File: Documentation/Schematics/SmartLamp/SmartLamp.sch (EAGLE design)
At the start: 31 parts, among them J2 AVR_SPI_PROG_5X2PTH2, Q1 STN4NF03L, Q2 STN4NF03L, Q3 STN4NF03L, U1 MIC2920A, U2 DS3231MZ, U3 ATMEGA8/168/328, U4 HM-10

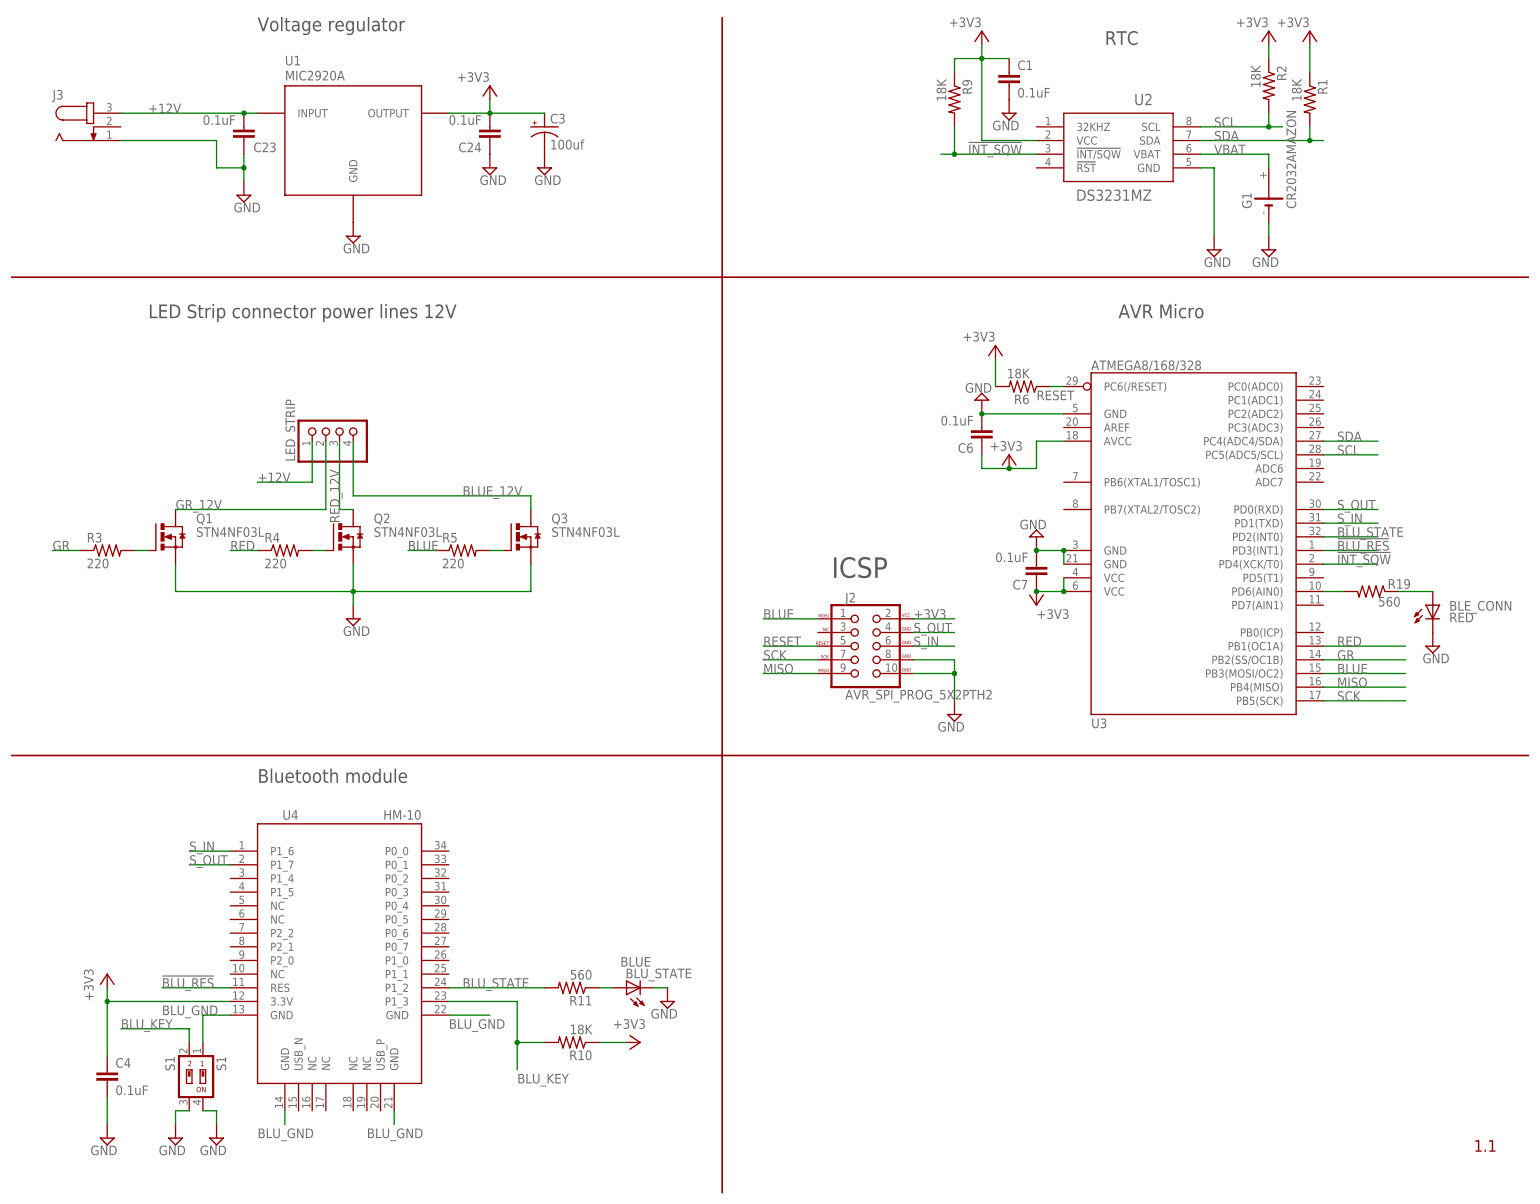
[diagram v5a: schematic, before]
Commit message: Fixed RX/?TX connection from micro to the BLE module.
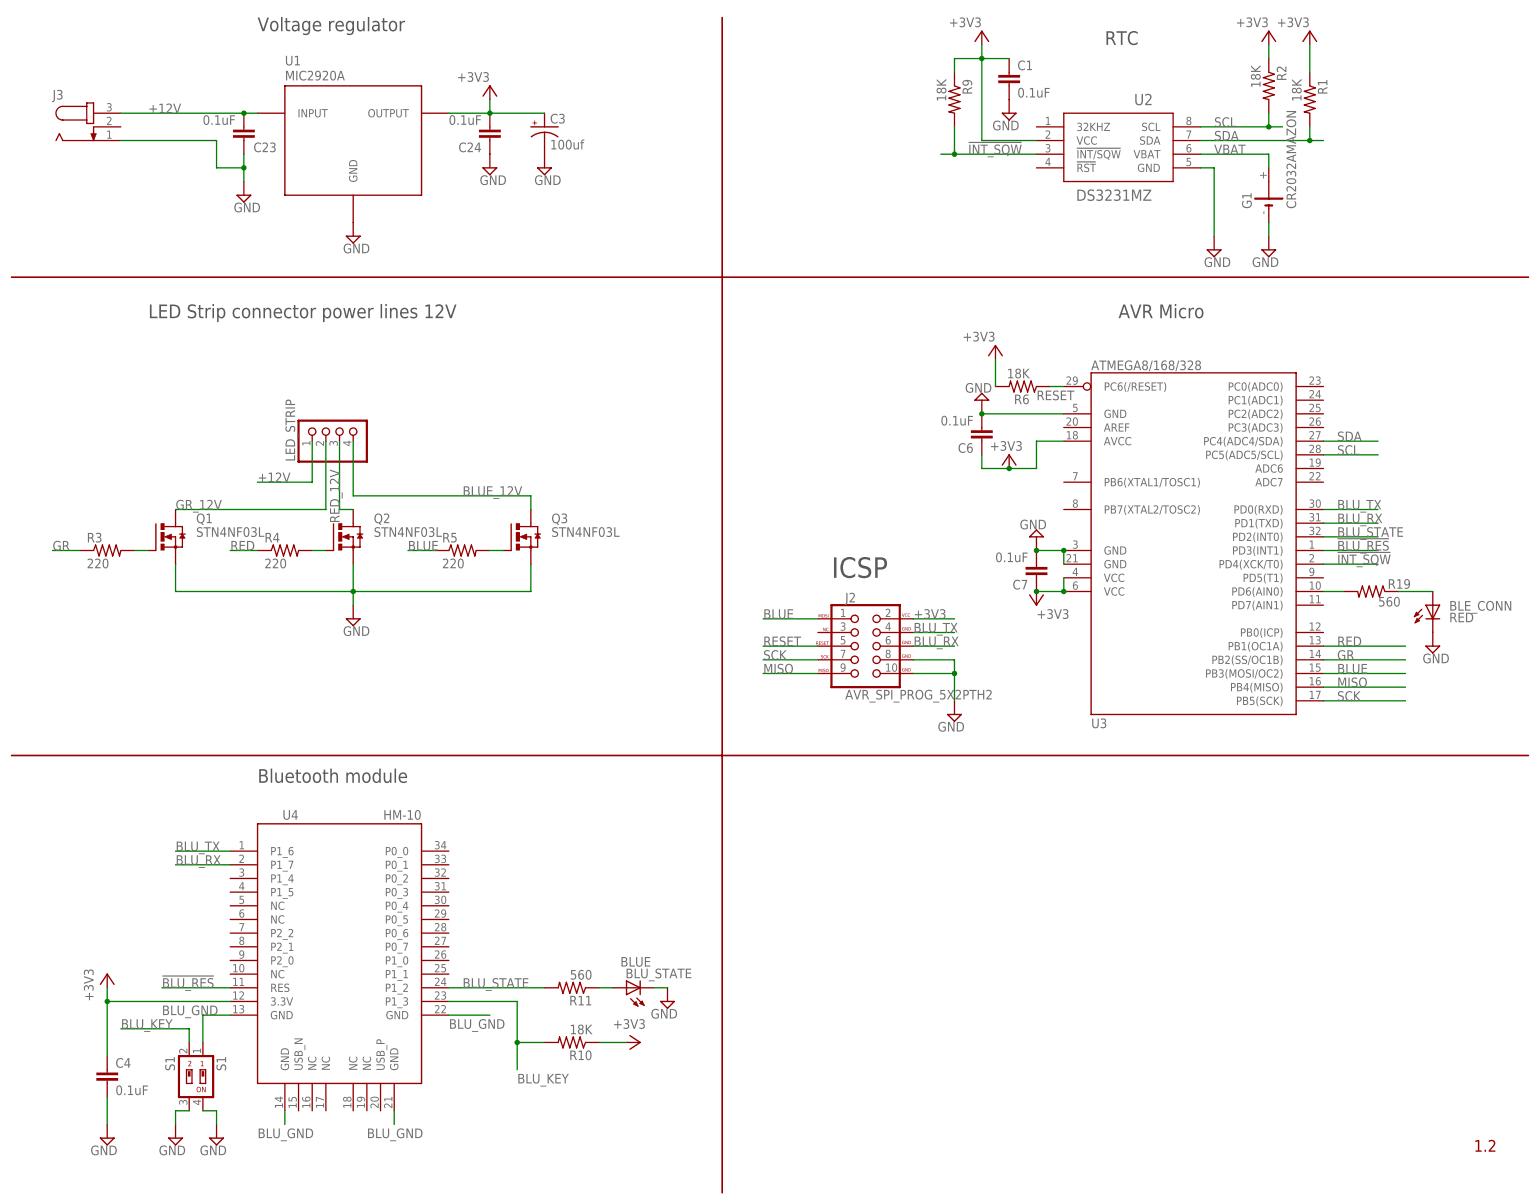
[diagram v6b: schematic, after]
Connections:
- removed net S_IN: J2.GND@2, U3.PD1(TXD), U4.P1_6
- removed net S_OUT: J2.GND@1, U3.PD0(RXD), U4.P1_7
- new net BLU_RX: J2.GND@2, U3.PD1(TXD), U4.P1_7
- new net BLU_TX: J2.GND@1, U3.PD0(RXD), U4.P1_6
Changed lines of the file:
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@@
 <schematic xreflabel="%F%N/%S" xrefpart="/%S.%C%R">
 <attributes>
-<attribute name="VERSION" value="1.1"/>
+<attribute name="VERSION" value="1.2"/>
 </attributes>
 <variantdefs>
@@
 </segment>
 </net>
-<net name="S_OUT" class="0">
-<segment>
-<pinref part="U4" gate="G$1" pin="P1_7"/>
-<wire x1="121.92" y1="66.04" x2="114.3" y2="66.04" width="0.1524" layer="91"/>
-<label x="114.3" y="66.04" size="1.778" layer="95" font="vector"/>
-</segment>
-<segment>
-<pinref part="U3" gate="G$1" pin="PD0(RXD)"/>
-<wire x1="325.12" y1="132.08" x2="335.28" y2="132.08" width="0.1524" layer="91"/>
-<label x="327.66" y="132.08" size="1.778" layer="95" font="vector"/>
-</segment>
-<segment>
-<pinref part="J2" gate="G$1" pin="GND@1"/>
-<wire x1="248.92" y1="109.22" x2="256.54" y2="109.22" width="0.1524" layer="91"/>
-<label x="248.92" y="109.22" size="1.778" layer="95" font="vector"/>
-</segment>
-</net>
 <net name="SCK" class="0">
 <segment>
@@
 <wire x1="345.44" y1="116.84" x2="339.09" y2="116.84" width="0.1524" layer="91"/>
 <pinref part="BLE_CONN" gate="G$1" pin="A"/>
-</segment>
-</net>
-<net name="S_IN" class="0">
-<segment>
-<pinref part="U4" gate="G$1" pin="P1_6"/>
-<wire x1="121.92" y1="68.58" x2="114.3" y2="68.58" width="0.1524" layer="91"/>
-<label x="114.3" y="68.58" size="1.778" layer="95" font="vector"/>
-</segment>
-<segment>
-<pinref part="U3" gate="G$1" pin="PD1(TXD)"/>
-<wire x1="325.12" y1="129.54" x2="335.28" y2="129.54" width="0.1524" layer="91"/>
-<label x="327.66" y="129.54" size="1.778" layer="95" font="vector"/>
-</segment>
-<segment>
-<pinref part="J2" gate="G$1" pin="GND@2"/>
-<wire x1="248.92" y1="106.68" x2="256.54" y2="106.68" width="0.1524" layer="91"/>
-<label x="248.92" y="106.68" size="1.778" layer="95" font="vector"/>
 </segment>
 </net>
@@
 </segment>
 </net>
+<net name="BLU_TX" class="0">
+<segment>
+<pinref part="U4" gate="G$1" pin="P1_6"/>
+<wire x1="121.92" y1="68.58" x2="111.76" y2="68.58" width="0.1524" layer="91"/>
+<label x="111.76" y="68.58" size="1.778" layer="95" font="vector"/>
+</segment>
+<segment>
+<pinref part="U3" gate="G$1" pin="PD0(RXD)"/>
+<wire x1="325.12" y1="132.08" x2="335.28" y2="132.08" width="0.1524" layer="91"/>
+<label x="327.66" y="132.08" size="1.778" layer="95" font="vector"/>
+</segment>
+<segment>
+<pinref part="J2" gate="G$1" pin="GND@1"/>
+<wire x1="248.92" y1="109.22" x2="256.54" y2="109.22" width="0.1524" layer="91"/>
+<label x="248.92" y="109.22" size="1.778" layer="95" font="vector"/>
+</segment>
+</net>
+<net name="BLU_RX" class="0">
+<segment>
+<pinref part="U4" gate="G$1" pin="P1_7"/>
+<wire x1="121.92" y1="66.04" x2="111.76" y2="66.04" width="0.1524" layer="91"/>
+<label x="111.76" y="66.04" size="1.778" layer="95" font="vector"/>
+</segment>
+<segment>
+<pinref part="U3" gate="G$1" pin="PD1(TXD)"/>
+<wire x1="325.12" y1="129.54" x2="335.28" y2="129.54" width="0.1524" layer="91"/>
+<label x="327.66" y="129.54" size="1.778" layer="95" font="vector"/>
+</segment>
+<segment>
+<pinref part="J2" gate="G$1" pin="GND@2"/>
+<wire x1="248.92" y1="106.68" x2="256.54" y2="106.68" width="0.1524" layer="91"/>
+<label x="248.92" y="106.68" size="1.778" layer="95" font="vector"/>
+</segment>
+</net>

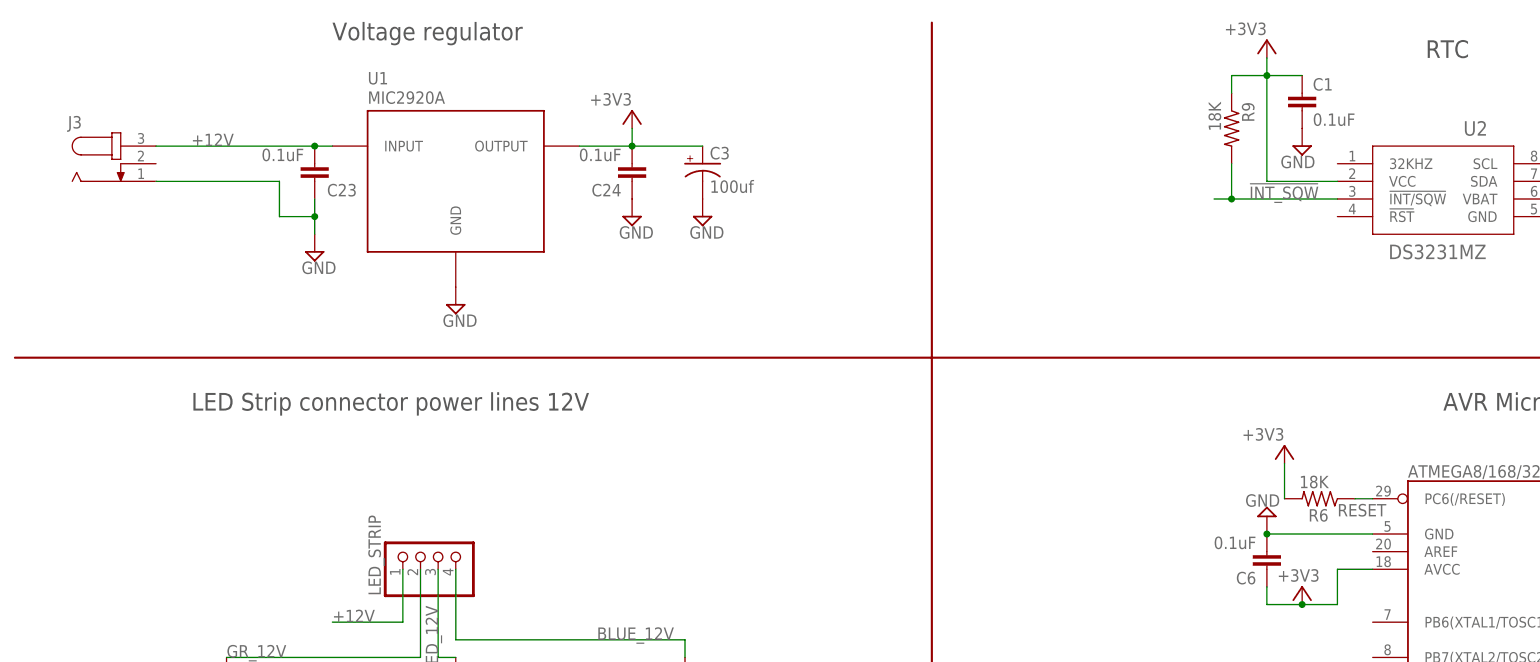
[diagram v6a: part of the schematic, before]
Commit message: Added micro reset button.
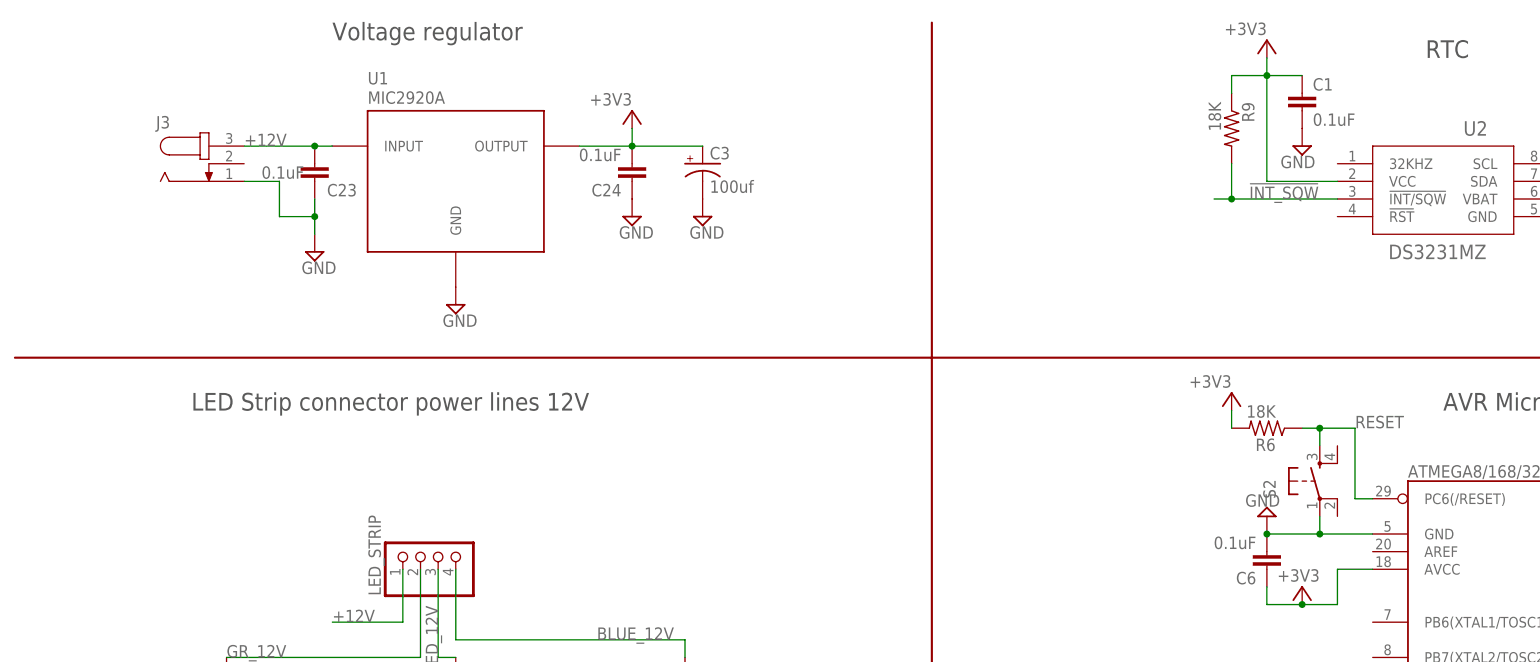
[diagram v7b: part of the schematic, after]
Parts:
- added S2: DTSM-6, switch-tact:DTSM-6
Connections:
- net GND: now also S2.1
- net RESET: now also S2.3
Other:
- moved on the sheet: J3, R6
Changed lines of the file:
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@@
 <part name="GND5" library="supply2" deviceset="GND" device=""/>
 <part name="J3" library="con-jack" deviceset="JACK-PLUG" device="0"/>
+<part name="S2" library="switch-tact" deviceset="DTSM-6" device=""/>
 </parts>
 <sheets>
@@
 <instance part="C23" gate="G$1" x="124.46" y="200.66" smashed="yes" rot="R180">
 <attribute name="NAME" x="130.556" y="200.279" size="1.778" layer="95" rot="R180"/>
-<attribute name="VALUE" x="122.936" y="205.359" size="1.778" layer="96" rot="R180"/>
+<attribute name="VALUE" x="122.936" y="202.819" size="1.778" layer="96" rot="R180"/>
 </instance>
 <instance part="C24" gate="G$1" x="170.18" y="200.66" rot="R180"/>
@@
 <instance part="Q2" gate="G$1" x="142.24" y="127"/>
 <instance part="Q3" gate="G$1" x="175.26" y="127"/>
-<instance part="R6" gate="G$1" x="269.24" y="154.94" smashed="yes" rot="R180">
-<attribute name="NAME" x="270.51" y="153.4414" size="1.778" layer="95" rot="R180"/>
-<attribute name="VALUE" x="270.51" y="158.242" size="1.778" layer="96" rot="R180"/>
-</instance>
-<instance part="+3V1" gate="G$1" x="264.16" y="162.56" smashed="yes">
-<attribute name="VALUE" x="264.16" y="165.1" size="1.778" layer="96" rot="R180"/>
+<instance part="R6" gate="G$1" x="261.62" y="165.1" smashed="yes" rot="R180">
+<attribute name="NAME" x="262.89" y="163.6014" size="1.778" layer="95" rot="R180"/>
+<attribute name="VALUE" x="262.89" y="168.402" size="1.778" layer="96" rot="R180"/>
+</instance>
+<instance part="+3V1" gate="G$1" x="256.54" y="170.18" smashed="yes">
+<attribute name="VALUE" x="256.54" y="172.72" size="1.778" layer="96" rot="R180"/>
 </instance>
 <instance part="C3" gate="G$1" x="180.34" y="203.2"/>
@@
 <instance part="J2" gate="G$1" x="238.76" y="106.68"/>
 <instance part="GND5" gate="GND" x="256.54" y="93.98" rot="MR0"/>
-<instance part="J3" gate="G$1" x="96.52" y="203.2"/>
+<instance part="J3" gate="G$1" x="109.22" y="203.2"/>
+<instance part="S2" gate="G$1" x="269.24" y="157.48" smashed="yes">
+<attribute name="NAME" x="262.89" y="154.94" size="1.778" layer="95" rot="R90"/>
+</instance>
 </instances>
 <busses>
@@
 <wire x1="119.38" y1="195.58" x2="124.46" y2="195.58" width="0.1524" layer="91"/>
 <pinref part="J3" gate="G$1" pin="1"/>
-<wire x1="119.38" y1="200.66" x2="101.6" y2="200.66" width="0.1524" layer="91"/>
+<wire x1="119.38" y1="200.66" x2="114.3" y2="200.66" width="0.1524" layer="91"/>
 </segment>
 <segment>
@@
 <segment>
 <pinref part="U3" gate="G$1" pin="GND"/>
-<wire x1="276.86" y1="149.86" x2="261.62" y2="149.86" width="0.1524" layer="91"/>
+<wire x1="276.86" y1="149.86" x2="269.24" y2="149.86" width="0.1524" layer="91"/>
 <pinref part="SUPPLY20" gate="GND" pin="GND"/>
 <pinref part="C6" gate="G$1" pin="2"/>
 <junction x="261.62" y="149.86"/>
+<pinref part="S2" gate="G$1" pin="1"/>
+<wire x1="269.24" y1="149.86" x2="261.62" y2="149.86" width="0.1524" layer="91"/>
+<wire x1="269.24" y1="152.4" x2="269.24" y2="149.86" width="0.1524" layer="91"/>
+<junction x="269.24" y="149.86"/>
 </segment>
 <segment>
@@
 <net name="RESET" class="0">
 <segment>
-<pinref part="U3" gate="G$1" pin="PC6(/RESET)"/>
-<label x="271.78" y="152.4" size="1.778" layer="95"/>
-<pinref part="R6" gate="G$1" pin="1"/>
-<wire x1="274.32" y1="154.94" x2="276.86" y2="154.94" width="0.1524" layer="91"/>
-</segment>
-<segment>
 <pinref part="J2" gate="G$1" pin="RESET"/>
 <wire x1="231.14" y1="106.68" x2="220.98" y2="106.68" width="0.1524" layer="91"/>
 <label x="220.98" y="106.68" size="1.778" layer="95" font="vector"/>
+</segment>
+<segment>
+<pinref part="R6" gate="G$1" pin="1"/>
+<pinref part="S2" gate="G$1" pin="3"/>
+<wire x1="266.7" y1="165.1" x2="269.24" y2="165.1" width="0.1524" layer="91"/>
+<wire x1="269.24" y1="165.1" x2="269.24" y2="162.56" width="0.1524" layer="91"/>
+<wire x1="269.24" y1="165.1" x2="274.32" y2="165.1" width="0.1524" layer="91"/>
+<wire x1="274.32" y1="165.1" x2="274.32" y2="154.94" width="0.1524" layer="91"/>
+<junction x="269.24" y="165.1"/>
+<pinref part="U3" gate="G$1" pin="PC6(/RESET)"/>
+<wire x1="274.32" y1="154.94" x2="276.86" y2="154.94" width="0.1524" layer="91"/>
+<label x="274.32" y="165.1" size="1.778" layer="95" font="vector"/>
 </segment>
 </net>
@@
 <pinref part="+3V1" gate="G$1" pin="+3V3"/>
 <pinref part="R6" gate="G$1" pin="2"/>
-<wire x1="264.16" y1="160.02" x2="264.16" y2="154.94" width="0.1524" layer="91"/>
+<wire x1="256.54" y1="167.64" x2="256.54" y2="165.1" width="0.1524" layer="91"/>
 </segment>
 <segment>
@@
 </segment>
 <segment>
-<label x="106.68" y="205.74" size="1.778" layer="95" font="vector"/>
+<label x="114.3" y="205.74" size="1.778" layer="95" font="vector"/>
 <pinref part="C23" gate="G$1" pin="2"/>
 <wire x1="124.46" y1="205.74" x2="127" y2="205.74" width="0.1524" layer="91"/>
 <pinref part="U1" gate="G$1" pin="INPUT"/>
 <pinref part="J3" gate="G$1" pin="3"/>
-<wire x1="101.6" y1="205.74" x2="124.46" y2="205.74" width="0.1524" layer="91"/>
+<wire x1="114.3" y1="205.74" x2="124.46" y2="205.74" width="0.1524" layer="91"/>
 <junction x="124.46" y="205.74"/>
 </segment>
